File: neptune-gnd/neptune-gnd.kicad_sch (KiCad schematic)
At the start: 23 parts, among them J1 Micro_SD_Card_Det2, J2 SMA, SW1 Boot Option, SW2 EN, U1 ESP32-S3-WROOM-1U, U2 AP2112K-3.3, U3 RFM95W-868S2

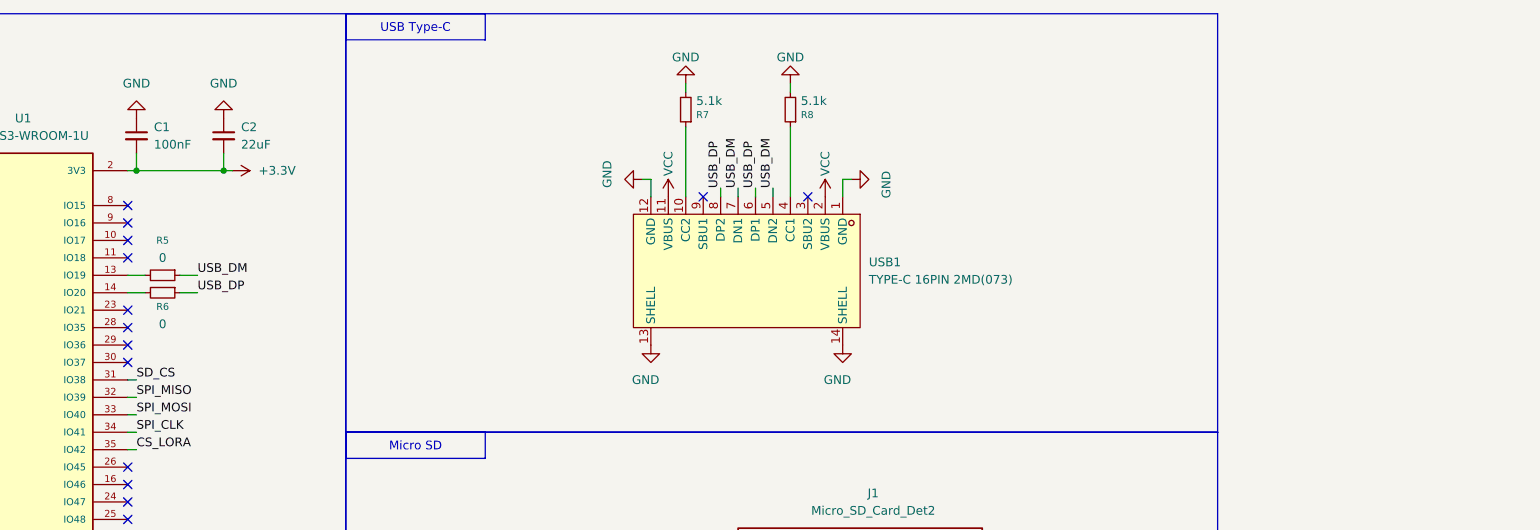
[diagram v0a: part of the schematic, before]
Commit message: fixing DRC problems, rerouting start
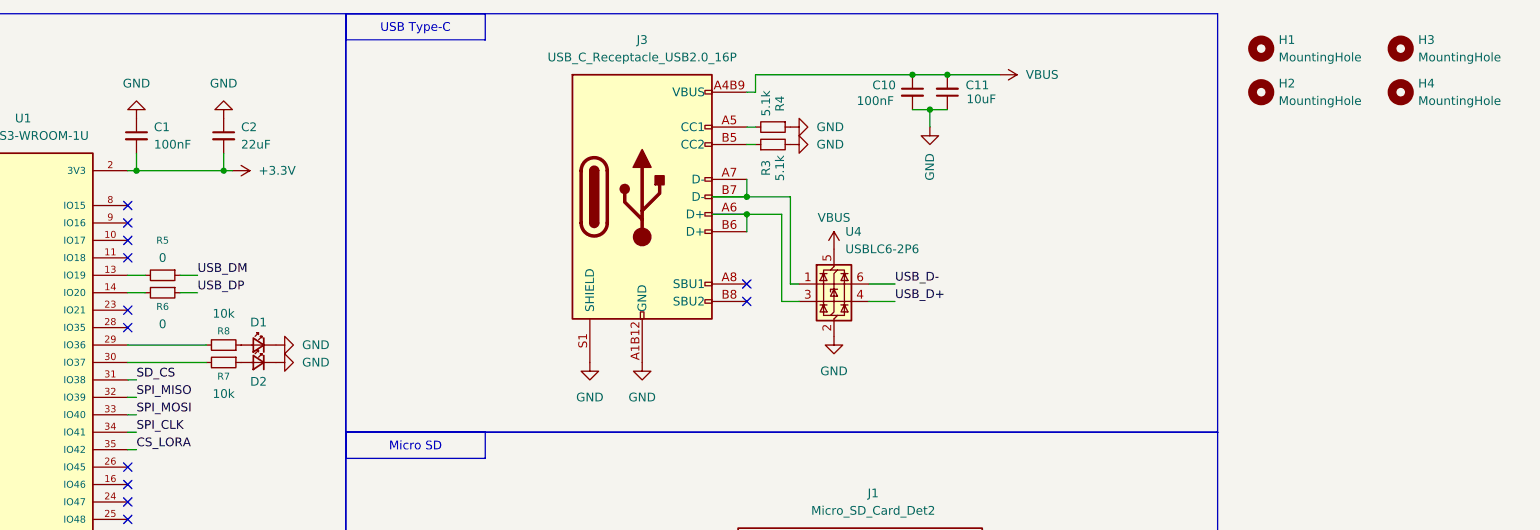
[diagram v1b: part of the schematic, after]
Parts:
- removed USB1: TYPE-C 16PIN 2MD(073), neptune-gnd:USB-C-SMD_TYPE-C-6PIN-2MD-073, symbol neptune-gnd:TYPE-C16PIN2MD(073)
- added C10: 100nF, Capacitor_SMD:C_0603_1608Metric, symbol Device:C_Small
- added C11: 10uF, Capacitor_SMD:C_0603_1608Metric, symbol Device:C_Small
- added D1, D2: LED_Small, LED_SMD:LED_0603_1608Metric, symbol Device:LED_Small
- added H1, H2, H3, H4: MountingHole, MountingHole:MountingHole_2.2mm_M2_DIN965_Pad_TopBottom, symbol Mechanical:MountingHole
- added J3: USB_C_Receptacle_USB2.0_16P, neptune-gnd:USB-SMD_TYPE-C-16PQT-073, symbol Connector:USB_C_Receptacle_USB2.0_16P
- added R3, R4: 5.1k, Resistor_SMD:R_0402_1005Metric, symbol Device:R_Small
- added U4: USBLC6-2P6, gaia_obc-footprints:SOT-666, symbol Power_Protection:USBLC6-2P6
- R7, R8: value 5.1k -> 10k; footprint Resistor_SMD:R_0402_1005Metric -> Resistor_SMD:R_0603_1608Metric
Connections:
- net GND: now also C10.2, C11.1, D1.1 (K), D2.1 (K), J3.A1B12 (GND), J3.B1A12 (GND), J3.S1 (SHIELD), R3.2, R4.1, U4.2 (GND); no longer R7.2, R8.2
- net at R8.1: now also D1.2 (A)
- net at U1.29 (IO36): now also R8.2
- net at U1.30 (IO37): now also R7.2
- net at R7.1: now also D2.2 (A)
- new net: J3.A7 (D-), J3.B7 (D-), U4.1 (I/O1)
- new net: J3.A6 (D+), J3.B6 (D+), U4.3 (I/O2)
- new net: J3.A5 (CC1), R4.2
- new net: J3.B5 (CC2), R3.1
- new net USB_D+: U4.4 (I/O2)
- new net USB_D-: U4.6 (I/O1)
- new net VBUS: C10.1, C11.2, J3.A4B9 (VBUS), J3.B4A9 (VBUS), U4.5 (VBUS)
- no-connect marks 39 -> 37

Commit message: send to production
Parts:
- removed U4: USBLC6-2P6, gaia_obc-footprints:SOT-666, symbol Power_Protection:USBLC6-2P6
- added R10, R9: 10k, Resistor_SMD:R_0603_1608Metric, symbol Device:R_Small
- added SW3: SW_Slide_DPDT, neptune-gnd:MS-22D28-G020, symbol Switch:SW_Slide_DPDT
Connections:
- net USB_DM is gone; now on net USB_DN: R5.1
- net VBUS is gone; now on net VCC: C10.1, C11.2, J3.A4B9 (VBUS), J3.B4A9 (VBUS)
- net +3.3V: now also SW3.2 (B), SW3.5 (B)
- net USB_DP: now also J3.A6 (D+), J3.B6 (D+)
- net USB_DN: now reaches J3.A7 (D-), J3.B7 (D-)
- net at U1.4 (IO4): now also R10.2
- net at U1.5 (IO5): now also R9.1
- new net RX: R9.2, SW3.3 (C), SW3.4 (A)
- new net TX: R10.1, SW3.1 (A), SW3.6 (C)
- no-connect marks 37 -> 35
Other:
- moved on the sheet: C4, R2, SW2

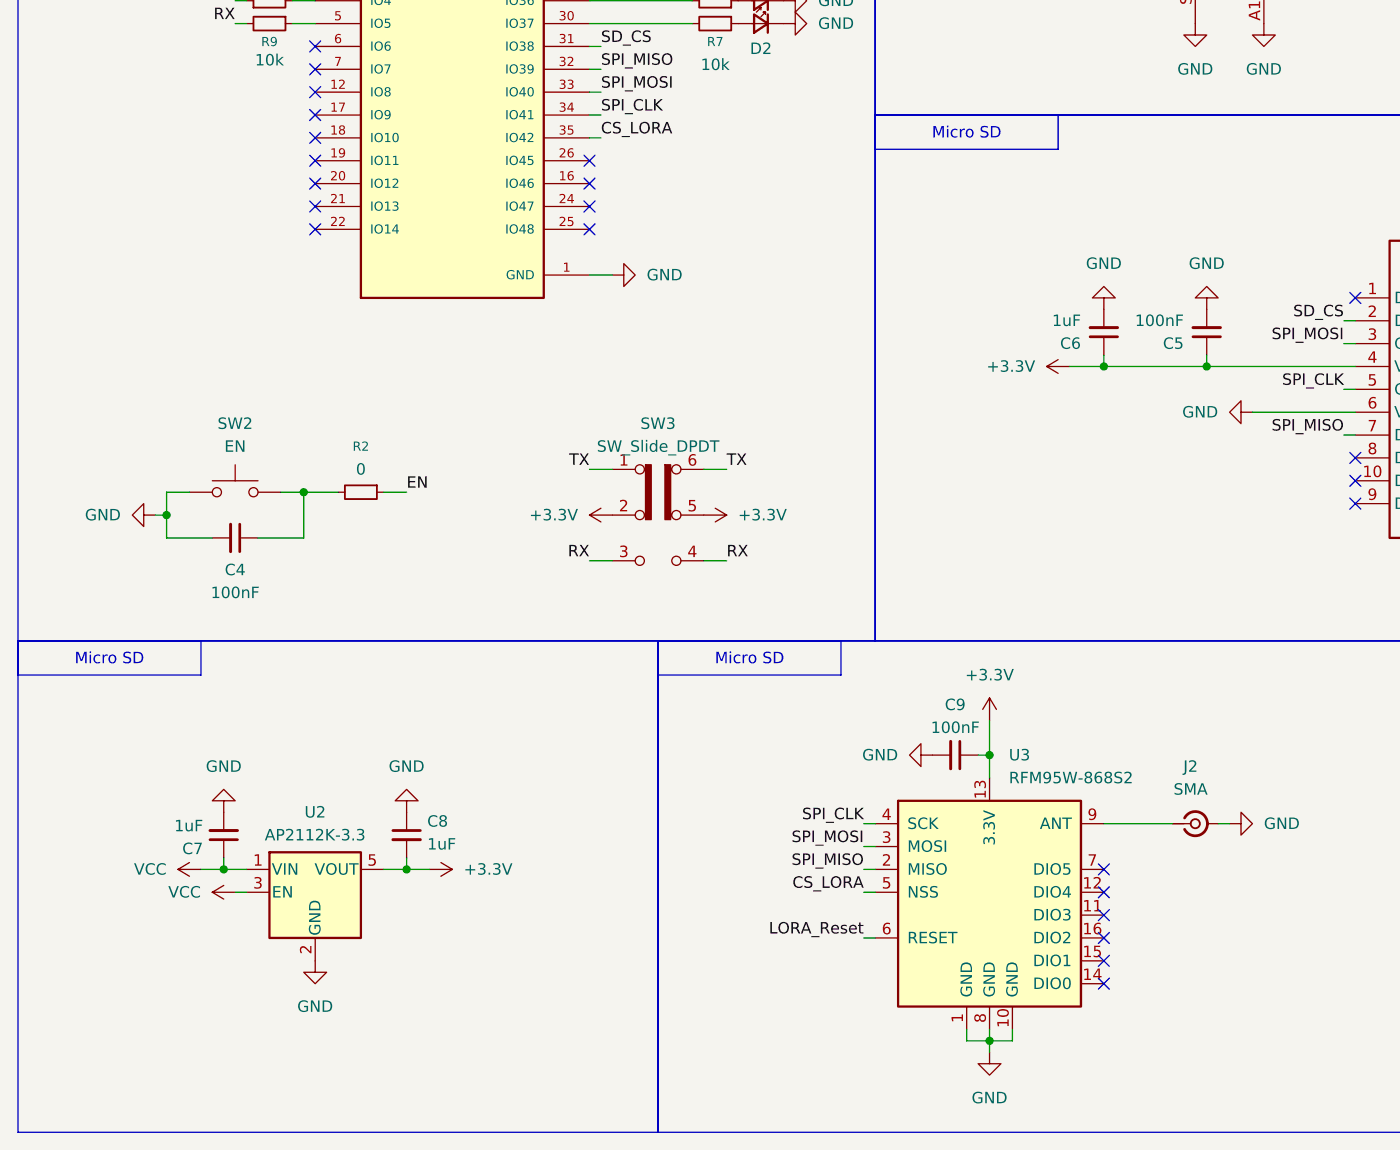
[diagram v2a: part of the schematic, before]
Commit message: v1.1 - adding interrupt conn
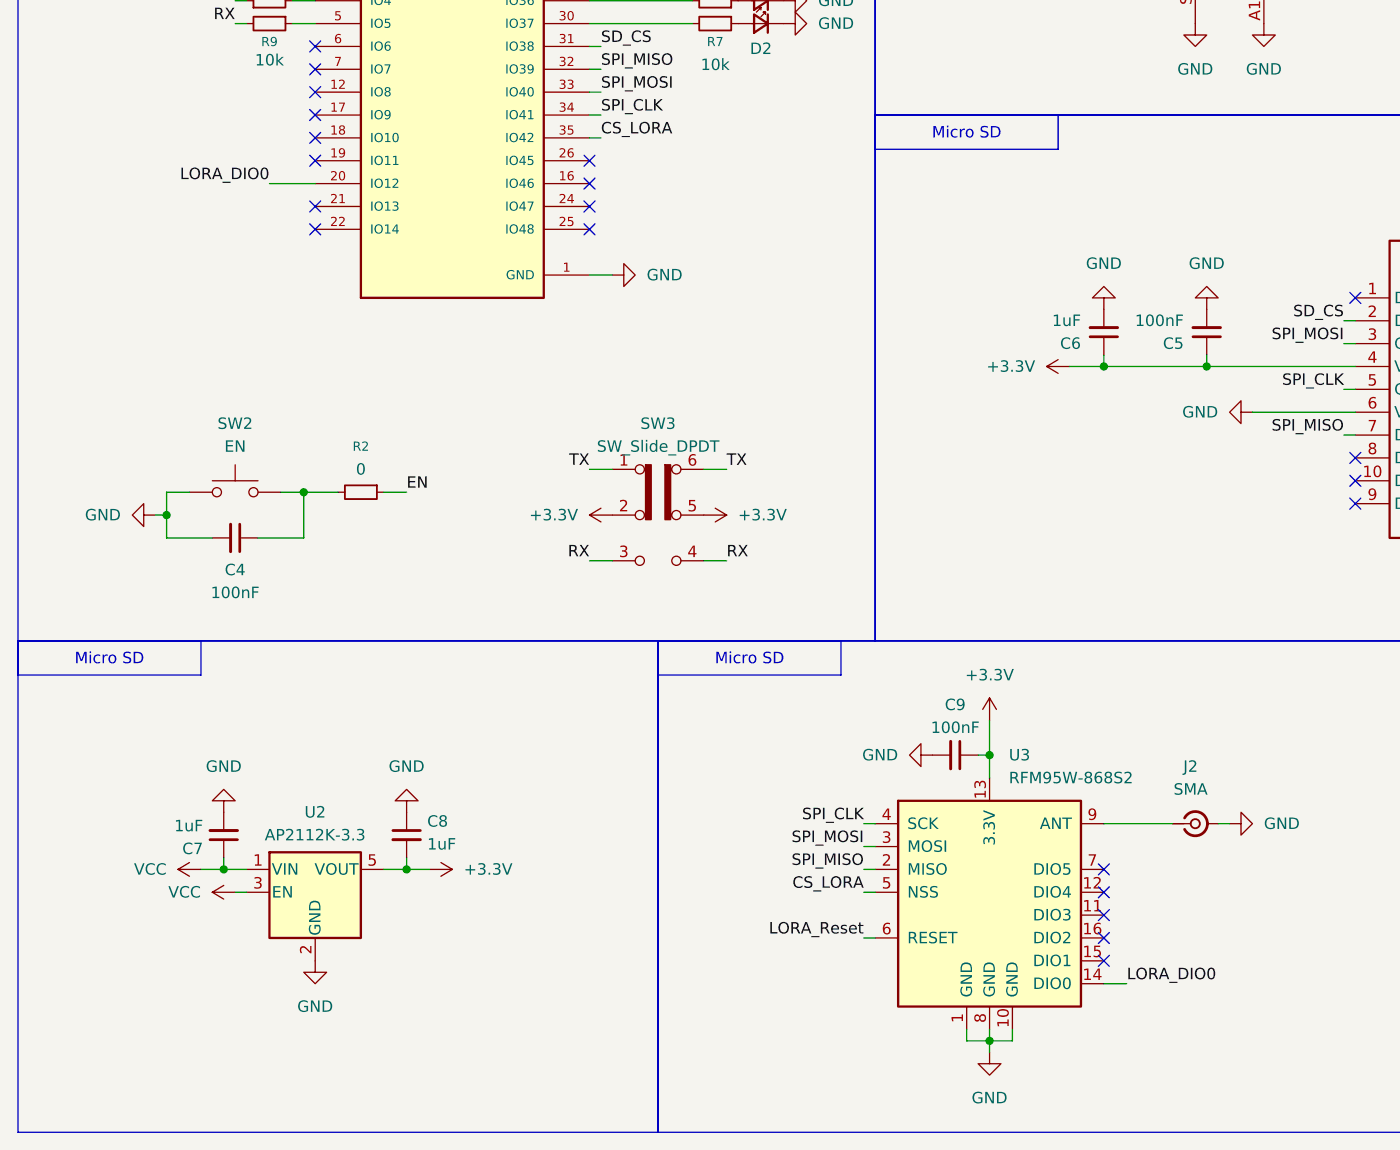
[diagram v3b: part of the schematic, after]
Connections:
- net LORA_DIO0: now reaches U1.20 (IO12)
- net LORA_DIO0: now also U3.14 (DIO0)
- no-connect marks 35 -> 33
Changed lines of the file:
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@@
-	)
-	(no_connect
-		(at 50.8 85.09)
 	)
 	(no_connect
@@
 	)
 	(no_connect
-		(at 138.43 173.99)
-	)
-	(no_connect
 		(at 50.8 57.15)
 	)
@@
 	(wire
 		(pts
+			(xy 140.97 173.99) (xy 138.43 173.99)
+		)
+		(stroke
+			(width 0)
+			(type default)
+		)
+	)
+	(wire
+		(pts
 			(xy 81.28 39.37) (xy 82.55 39.37)
 		)
@@
 		(pts
 			(xy 60.96 161.29) (xy 63.5 161.29)
+		)
+		(stroke
+			(width 0)
+			(type default)
+		)
+	)
+	(wire
+		(pts
+			(xy 45.72 85.09) (xy 50.8 85.09)
 		)
 		(stroke
@@
 		)
 	)
+	(label "LORA_DIO0"
+		(at 45.72 85.09 180)
+		(effects
+			(font
+				(size 1.27 1.27)
+			)
+			(justify right bottom)
+		)
+	)
 	(label "RX"
 		(at 41.91 67.31 180)
@@
 		)
 	)
+	(label "LORA_DIO0"
+		(at 140.97 173.99 0)
+		(effects
+			(font
+				(size 1.27 1.27)
+			)
+			(justify left bottom)
+		)
+	)
